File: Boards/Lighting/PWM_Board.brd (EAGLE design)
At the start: 70.8 x 69.8 mm, 54 parts, among them Q1 N-FET, Q10 N-FET, Q11 N-FET, Q12 N-FET, Q13 N-FET, Q14 N-FET, Q15 N-FET, Q16 N-FET, Q17 N-FET, Q18 N-FET, Q19 N-FET, Q2 N-FET, Q20 N-FET, Q21 N-FET, Q22 N-FET, Q23 N-FET, Q24 N-FET, Q25 N-FET, Q26 N-FET, Q27 N-FET, Q28 N-FET, Q29 N-FET, Q3 N-FET, Q30 N-FET, Q31 N-FET, Q32 N-FET, Q4 N-FET, Q5 N-FET, Q6 N-FET, Q7 N-FET, Q8 N-FET, Q9 N-FET

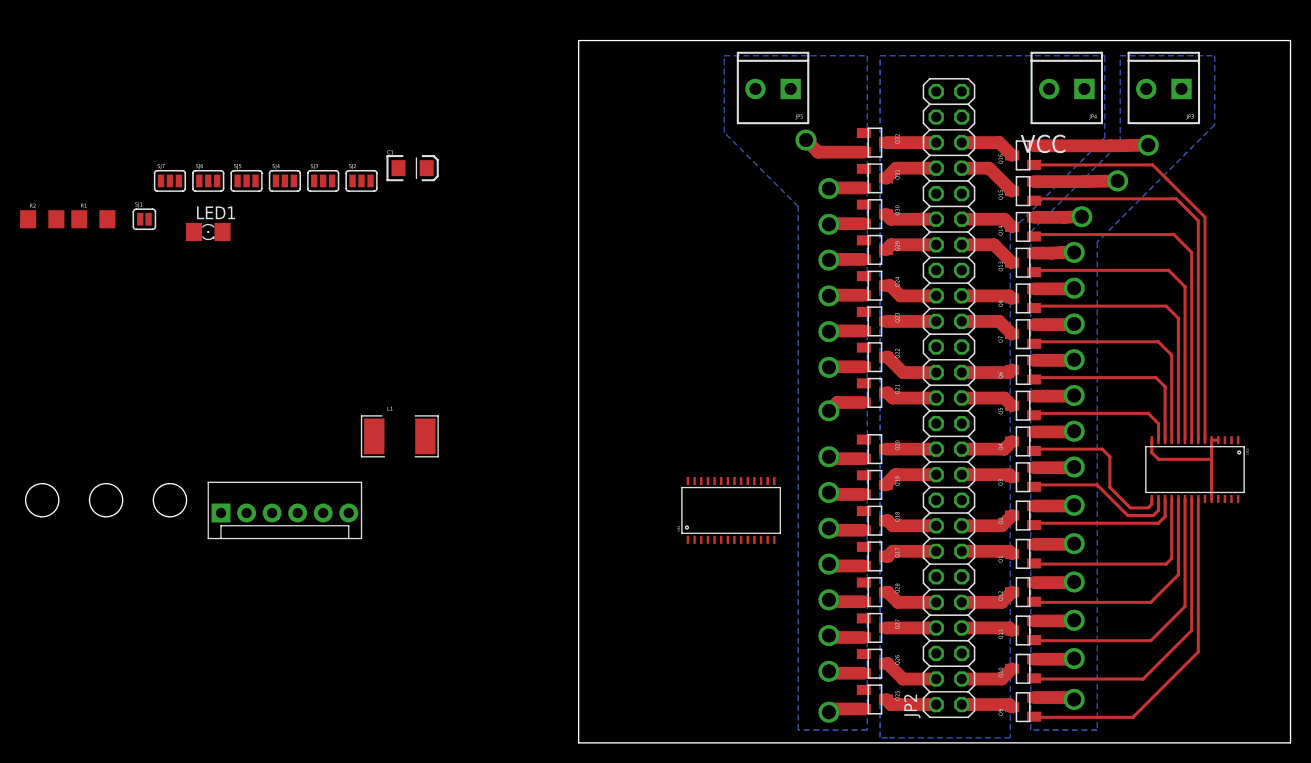
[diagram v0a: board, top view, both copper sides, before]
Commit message: Finished PWM lighting board, now uses a ribbon cable to connect to a break out terminal board
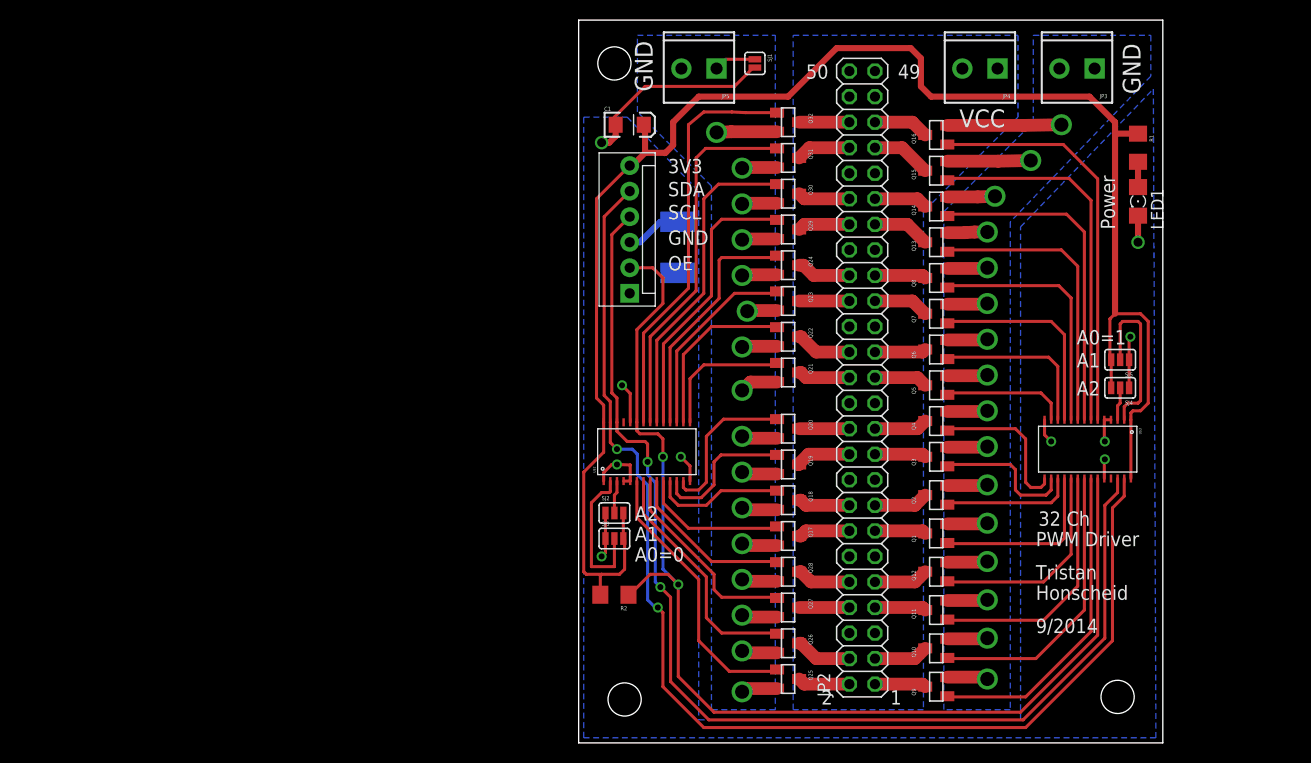
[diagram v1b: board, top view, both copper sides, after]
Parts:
- removed SJ6, SJ7: (no value), 1_SparkFun-Passives:SJ_3
- removed U$1: PCA9685, 0_Tristan's_Lib:TSSOP28
- added U$2: PCA9685, 0_Tristan's_Lib:TSSOP28
- moved R1 104.1 mm to (55.6, 59.2), turned to 270 degrees
- moved STANDOFF3 102.5 mm to (53.6, 4.57)
- moved LED1 92.5 mm to (55.6, 53.8), turned to 270 degrees
- moved SJ5 88.7 mm to (53.8, 38.1), turned to 180 degrees
- moved SJ4 85.6 mm to (53.8, 35.3), turned to 180 degrees
- moved STANDOFF4 71.6 mm to (3.56, 67.6)
- moved R2 68.1 mm to (3.56, 14.7), turned to 180 degrees
- moved SJ1 62.7 mm to (17.5, 67.6), turned to 270 degrees
- moved STANDOFF1 49.4 mm to (4.57, 4.32)
- moved JP1 46.1 mm to (5.08, 44.7), turned to 90 degrees
- moved SJ3 45.9 mm to (3.56, 20.3)
- moved SJ2 41.5 mm to (3.56, 22.9)
- moved L1 33.5 mm to (9.91, 49.3), flipped to the bottom, turned to 270 degrees
- moved C1 22.0 mm to (5.08, 61.5)
- moved U$3 10.9 mm to (50.3, 29.2)
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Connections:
- removed net N$43: SJ7.2, U$1.1
- removed net N$46: SJ6.2, U$3.1
- net 3.3V: now also U$2.28, U$3.1; no longer SJ6.3, SJ7.3, U$1.28
- net GND-ISO: now also U$2.1, U$2.14, U$2.24, U$2.4, U$2.5; no longer SJ6.1, SJ7.1, U$1.14, U$1.24, U$1.4, U$1.5
- net N$44: now also U$2.2; no longer U$1.2
- net N$45: now also U$2.3; no longer U$1.3
- net N1: now also U$2.6; no longer U$1.22
- net N10: now also U$2.16; no longer U$1.12
- net N11: now also U$2.17; no longer U$1.11
- net N12: now also U$2.18; no longer U$1.10
- net N13: now also U$2.19; no longer U$1.9
- net N14: now also U$2.20; no longer U$1.8
- net N15: now also U$2.21; no longer U$1.7
- net N16: now also U$2.22; no longer U$1.6
- net N2: now also U$2.7; no longer U$1.21
- net N3: now also U$2.8; no longer U$1.20
- net N4: now also U$2.9; no longer U$1.19
- net N5: now also U$2.10; no longer U$1.18
- net N6: now also U$2.11; no longer U$1.17
- net N7: now also U$2.12; no longer U$1.16
- net N8: now also U$2.13; no longer U$1.15
- net N9: now also U$2.15; no longer U$1.13
- net OE: now also U$2.23; no longer U$1.23
- net SCL: now also U$2.26; no longer U$1.26
- net SDA: now also U$2.27; no longer U$1.27
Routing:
- net 3.3V: track 0.00 -> 166.4 mm
- net SDA: track 0.00 -> 120.4 mm, vias 0 -> 2
- net OE: track 0.00 -> 115.3 mm, vias 0 -> 2
- net SCL: track 0.00 -> 115.0 mm, vias 0 -> 2
- net N16: track 0.00 -> 40.7 mm
- net GND-ISO: track 14.0 -> 52.0 mm, vias 0 -> 10
- net N15: track 0.00 -> 36.6 mm
- net N14: track 0.00 -> 32.0 mm
- net N13: track 0.00 -> 28.1 mm
- net N1: track 0.00 -> 27.6 mm
- net N12: track 0.00 -> 24.1 mm
- net N2: track 0.00 -> 23.9 mm
- net N3: track 0.00 -> 20.0 mm
- net N11: track 0.00 -> 19.5 mm
- net N10: track 0.00 -> 17.2 mm
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- added copper zone on layer 16, net GND-ISO
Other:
- board size 70.8 x 69.8 mm -> 58.1 x 71.9 mm
- board text added: "1"
- board text added: "2"
- board text added: "32 Ch"
- board text added: "3V3"
- board text added: "49"
- board text added: "50"
- board text added: "9/2014"
- board text added: "A0=0"
- board text added: "A0=1"
- board text added: "A1"
- board text added: "A2"
- board text added: "GND"
- board text added: "Honscheid"
- board text added: "OE"
- board text added: "PWM Driver"
- board text added: "Power"
- board text added: "SCL"
- board text added: "SDA"
- board text added: "Tristan"
